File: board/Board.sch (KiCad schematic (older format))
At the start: 62 parts, among them J1 CONN_02X10, J10 CONN_01X03, J11 CONN_01X03, J12 CONN_01X02, J15 GS3, J16 GS3, J17 GS3, J18 GS2, J19 CONN_01X01, J2 CONN_01X03, J3 CONN_01X03, J4 CONN_01X03, J5 CONN_01X03, J6 CONN_01X03, J7 CONN_01X03, J8 CONN_01X03, J9 CONN_01X03, SW1 SW_Push, U1 STM32F410RBTx, U2 LF33ABDT-TR, U3 ICM-20689, U4 SN74LVC1G04, U5 MS5637, U6 MAG3110, Y1 25 MHz

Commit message: decouple cap
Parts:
- added C3: 100nF, Capacitors_SMD:C_0805_HandSoldering, symbol C
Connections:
- net GND: now also C3.2
- net VCC: now also C3.1

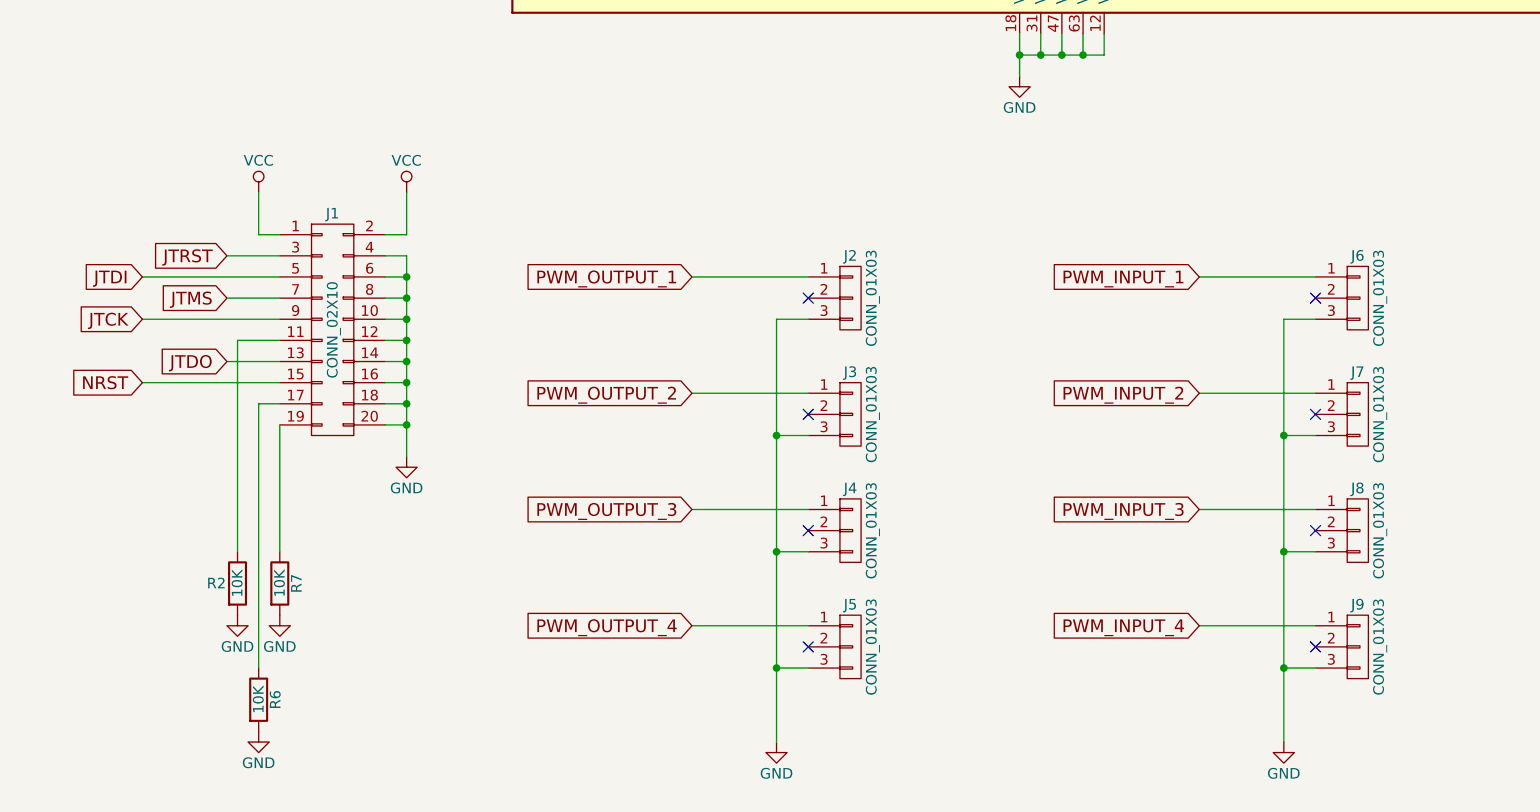
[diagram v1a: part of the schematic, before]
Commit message: smaller JTAG pin
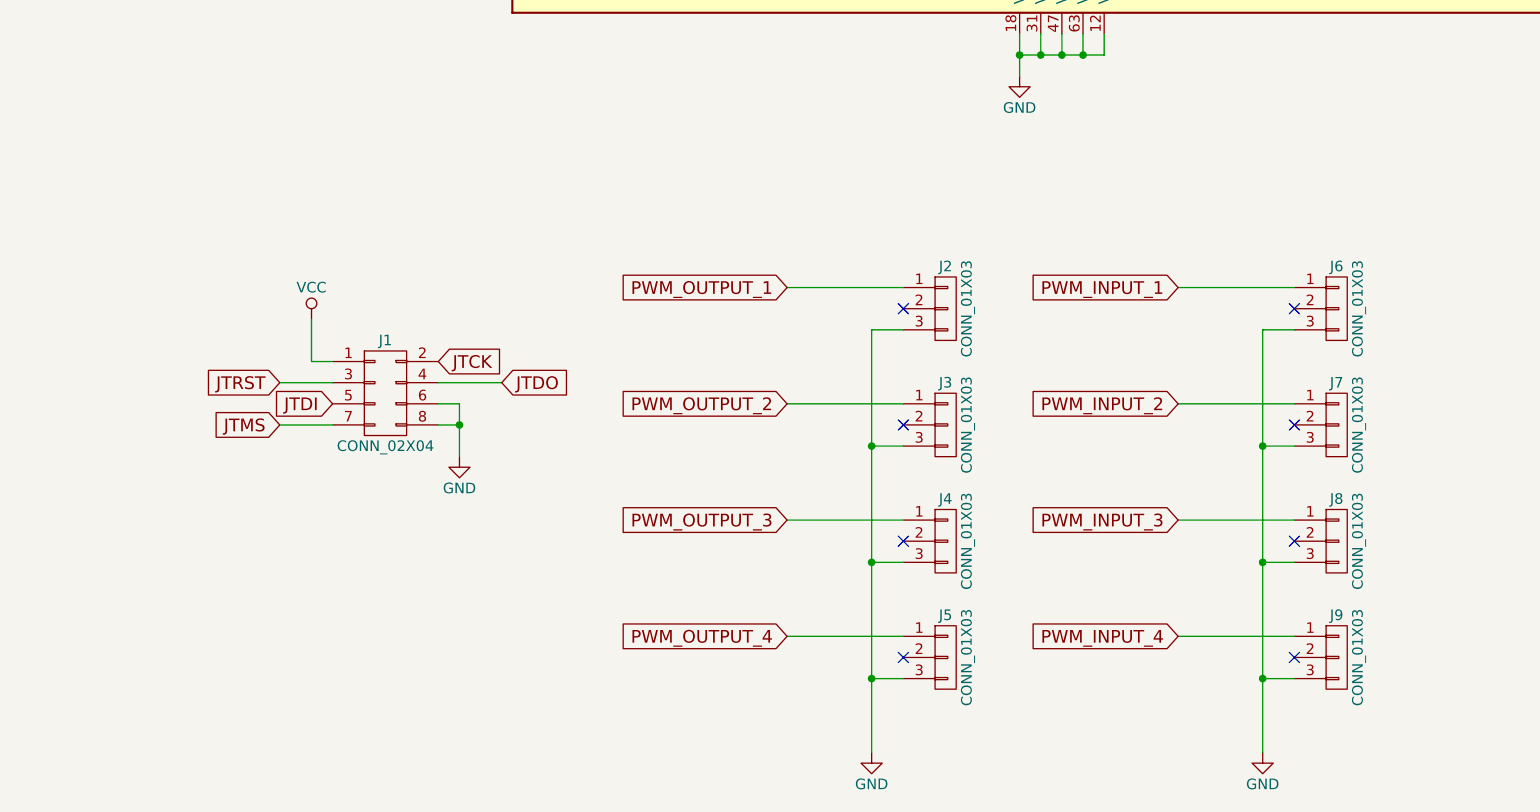
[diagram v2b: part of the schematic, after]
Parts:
- removed J1: CONN_02X10, Connect:IDC_Header_Straight_20pins, symbol CONN_02X10
- removed R2, R6, R7: 10K, Resistors_SMD:R_0805_HandSoldering, symbol R
- added J1: CONN_02X04, Pin_Headers:Pin_Header_Straight_2x04_Pitch2.54mm, symbol CONN_02X04
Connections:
- net GND: now also J1.6 (P6), J1.8 (P8)
- net JTCK: now also J1.2 (P2)
- net JTDI: now also J1.5 (P5)
- net JTDO: now also J1.4 (P4)
- net JTMS: now also J1.7 (P7)
- net JTRST: now also J1.3 (P3)
- net VCC: now also J1.1 (P1)
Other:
- moved on the sheet: J2, J3, J4, J5, J6, J7, J8, J9

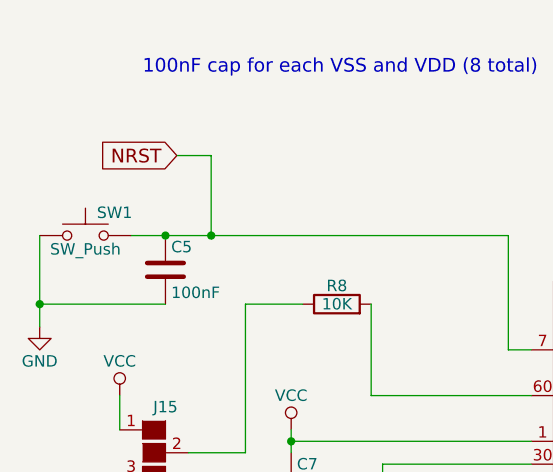
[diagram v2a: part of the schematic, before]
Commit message: removed NRST global labl
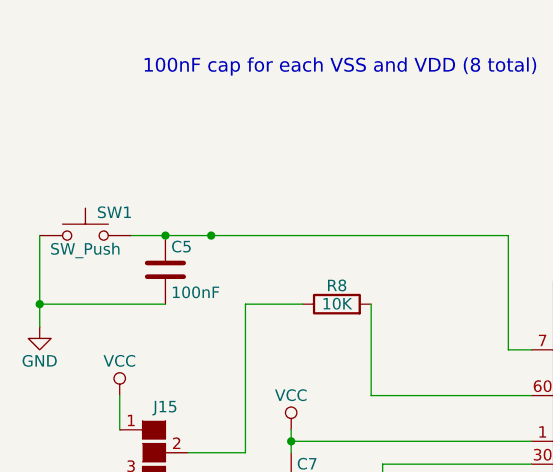
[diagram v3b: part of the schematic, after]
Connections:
- net NRST: no longer names the net of C5.1, SW1.2, U1.7 (NRST)

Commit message: new pcb
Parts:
- renumbered C16 to C10, C17 to C11, C18 to C12, C19 to C13, C3 to C14, C4 to C15, C20 to C16, C6 to C17, C21 to C18, C13 to C19, C22 to C20, C14 to C21, C23 to C22, C15 to C23, C5 to C3, C7 to C4, C9 to C5, C8 to C6, C10 to C7, C11 to C8, C12 to C9, J15 to J1, J9 to J10, J10 to J11, J17 to J12, J16 to J13, J12 to J14, J11 to J15, J18 to J16, J19 to J17, J1 to J2, J2 to J3, J3 to J4, J4 to J5, J5 to J6, J6 to J7, J7 to J8, J8 to J9, R3 to R2, R8 to R3, R9 to R4, R10 to R5, R11 to R6, R12 to R7, R4 to R8, R5 to R9, U4 to U2, U2 to U3, U3 to U4, U6 to U5, U5 to U6

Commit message: assigned the new footprint
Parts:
- U1: footprint Housings_QFP:LQFP-64_10x10mm_Pitch0.5mm -> Local_prints:LQFP-64_10x10mm_Pitch0.5mm_handsoldering

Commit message: organized the board a bit
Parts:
- added R10, R11: 10K, Resistors_SMD:R_0805_HandSoldering, symbol R
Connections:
- net VCC: now also R10.1, R11.1
- net I2C2_SCL: now reaches U1.29 (FMPI2C1_SCL/I2C2_SCL/I2S1_MCK/I2S2_CK/SPI2_SCK/PB10)
- net I2C2_SCL: now also U5.7 (SCL), U6.3 (SCL), R11.2
- net I2C2_SDA: now reaches U1.54 (ADC1_EXTI11/I2C2_SDA/I2S_CKIN/SYS_TRACED3/TIM5_CH4/PB11)
- net I2C2_SDA: now also U5.6 (SDA), U6.2 (SDA), R10.2
- net I2C_SCL renamed I2C1_SCL
- net I2C1_SCL: no longer U5.7 (SCL), U6.3 (SCL)
- net I2C_SDA renamed I2C1_SDA
- net I2C1_SDA: no longer U5.6 (SDA), U6.2 (SDA)
- no-connect marks 30 -> 28
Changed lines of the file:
@@
 $EndComp
 Text GLabel 8600 4550 2    60   Input ~ 0
-I2C_SDA
-Text GLabel 9050 4450 2    60   Input ~ 0
-I2C_SCL
+I2C1_SDA
+Text GLabel 9100 4450 2    60   Input ~ 0
+I2C1_SCL
 Text GLabel 8600 4350 2    60   Input ~ 0
 UART_RX
-Text GLabel 9050 4250 2    60   Input ~ 0
+Text GLabel 9100 4250 2    60   Input ~ 0
 UART_TX
 $Comp
@@
 $EndComp
 Text GLabel 9000 6850 0    60   Input ~ 0
-I2C_SDA
+I2C1_SDA
 Text GLabel 8500 6750 0    60   Input ~ 0
-I2C_SCL
+I2C1_SCL
 $Comp
 L GND #PWR027
@@
 	1    0    0    -1
 $EndComp
-NoConn ~ 8200 4650
 NoConn ~ 8200 3750
 NoConn ~ 8200 3650
@@
 NoConn ~ 2800 4950
 NoConn ~ 8200 3150
-NoConn ~ 8200 4750
 NoConn ~ 8200 4150
 Text GLabel 12950 4850 0    60   Input ~ 0
-I2C_SCL
+I2C2_SCL
 Text GLabel 13400 4750 0    60   Input ~ 0
-I2C_SDA
+I2C2_SDA
 $Comp
 L VCC #PWR037
@@
 MAG_INT
 Text GLabel 12850 6200 0    60   Input ~ 0
-I2C_SDA
+I2C2_SDA
 Text GLabel 12400 6100 0    60   Input ~ 0
-I2C_SCL
+I2C2_SCL
 $Comp
 L C C15
@@
 Wire Wire Line
 	14100 2650 15250 2650
-Connection ~ 1400 1450
 Wire Wire Line
 	1300 3850 2050 3850
@@
 	8200 4550 8600 4550
 Wire Wire Line
-	9050 4450 8200 4450
+	8200 4450 9100 4450
 Wire Wire Line
 	8200 4350 8600 4350
 Wire Wire Line
-	9050 4250 8200 4250
+	8200 4250 9100 4250
 Wire Wire Line
 	8500 6750 9250 6750
@@
 	2550 7400 2650 7400
 Connection ~ 2650 7400
+Text GLabel 10800 4750 2    60   Input ~ 0
+I2C2_SDA
+Wire Wire Line
+	8200 4650 11350 4650
+Text GLabel 11350 4650 2    60   Input ~ 0
+I2C2_SCL
+Wire Wire Line
+	8200 4750 10800 4750
+$Comp
+L R R11
+U 1 1 58FA170E
+P 10650 4300
+F 0 "R11" V 10730 4300 50  0000 C CNN
+F 1 "10K" V 10650 4300 50  0000 C CNN
+F 2 "Resistors_SMD:R_0805_HandSoldering" V 10580 4300 50  0001 C CNN
+F 3 "" H 10650 4300 50  0001 C CNN
+	1    10650 4300
+	1    0    0    -1
+$EndComp
+$Comp
+L R R10
+U 1 1 58FA180F
+P 10450 4300
+F 0 "R10" V 10530 4300 50  0000 C CNN
+F 1 "10K" V 10450 4300 50  0000 C CNN
+F 2 "Resistors_SMD:R_0805_HandSoldering" V 10380 4300 50  0001 C CNN
+F 3 "" H 10450 4300 50  0001 C CNN
+	1    10450 4300
+	1    0    0    -1
+$EndComp
+Wire Wire Line
+	10450 4450 10450 4750
+Connection ~ 10450 4750
+Wire Wire Line
+	10650 4450 10650 4650
+Connection ~ 10650 4650
+$Comp
+L VCC #PWR044
+U 1 1 58FA1F57
+P 10550 4000
+F 0 "#PWR044" H 10550 3850 50  0001 C CNN
+F 1 "VCC" H 10550 4150 50  0000 C CNN
+F 2 "" H 10550 4000 50  0001 C CNN
+F 3 "" H 10550 4000 50  0001 C CNN
+	1    10550 4000
+	1    0    0    -1
+$EndComp
+Wire Wire Line
+	10450 4150 10650 4150
+Wire Wire Line
+	10550 4150 10550 4000
+Connection ~ 10550 4150
 $EndSCHEMATC

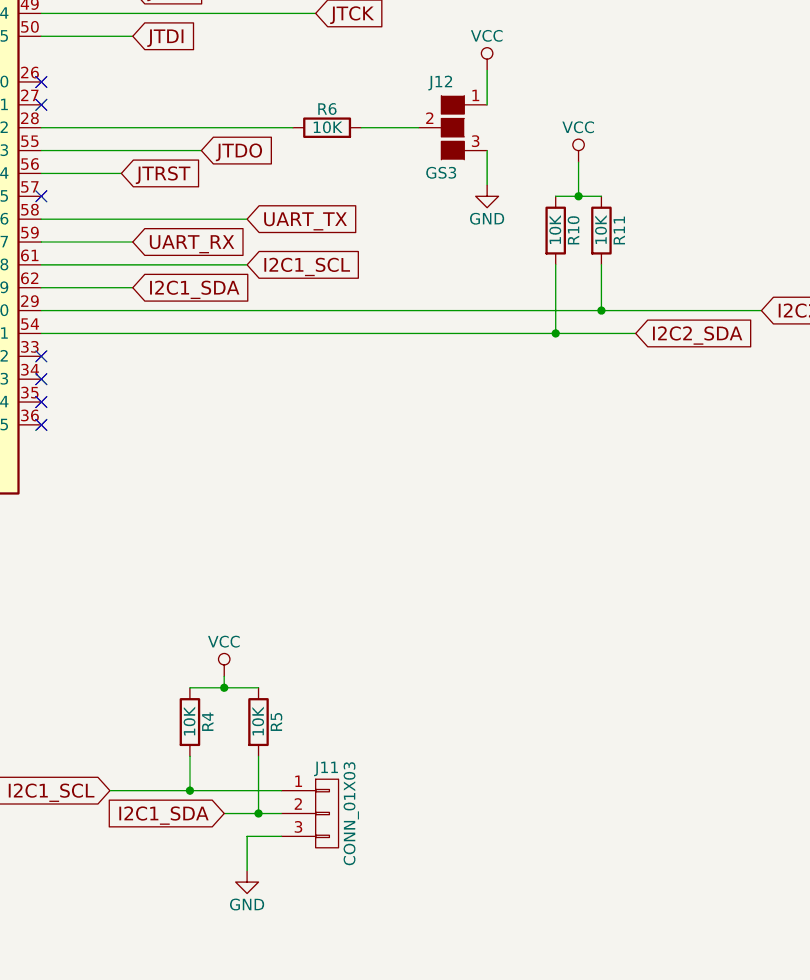
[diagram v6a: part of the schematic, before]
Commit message: using resistor array for I2C pullups
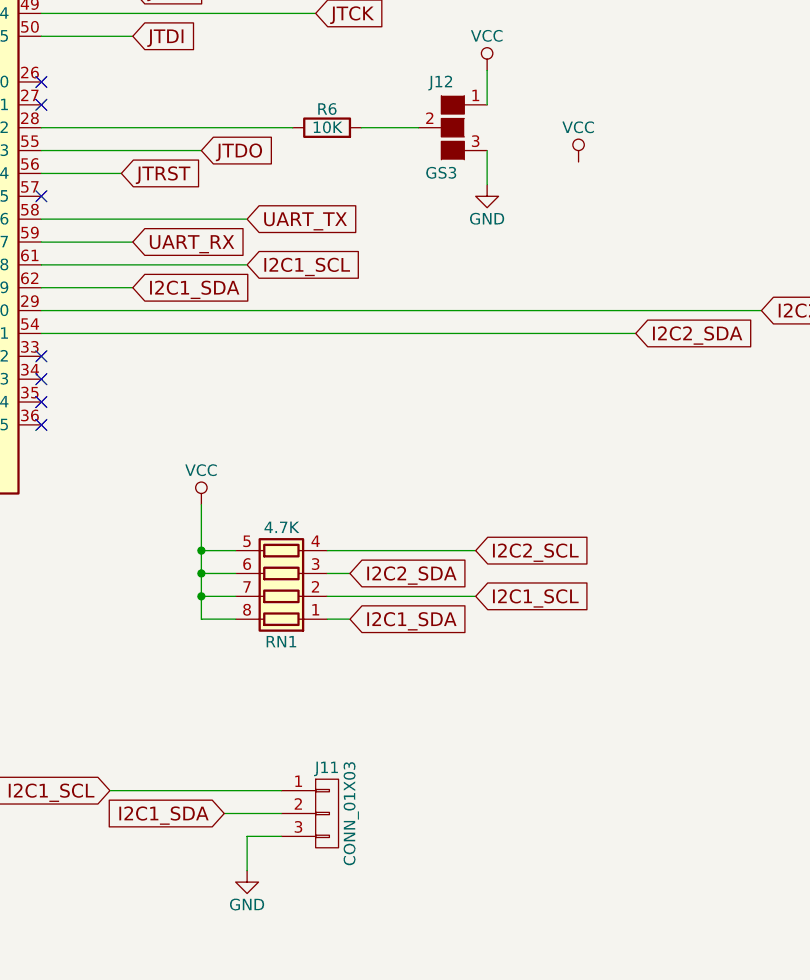
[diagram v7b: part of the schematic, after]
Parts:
- removed R10, R11, R4, R5: 10K, Resistors_SMD:R_0805_HandSoldering, symbol R
- added RN1: 4.7K, Resistors_SMD:R_Array_Convex_4x1206, symbol R_Pack04
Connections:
- net I2C1_SCL: now also RN1.2 (R2.1)
- net I2C1_SDA: now also RN1.1 (R1.1)
- net I2C2_SCL: now also RN1.4 (R4.1)
- net I2C2_SDA: now also RN1.3 (R3.1)
- net VCC: now also RN1.5 (R4.2), RN1.6 (R3.2), RN1.7 (R2.2), RN1.8 (R1.2)
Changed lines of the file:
@@
 UART_RX
 $Comp
-L R R4
-U 1 1 58D9A242
-P 8850 6450
-F 0 "R4" V 8930 6450 50  0000 C CNN
-F 1 "10K" V 8850 6450 50  0000 C CNN
-F 2 "Resistors_SMD:R_0805_HandSoldering" V 8780 6450 50  0001 C CNN
-F 3 "" H 8850 6450 50  0001 C CNN
-	1    8850 6450
-	1    0    0    -1
-$EndComp
-$Comp
-L R R5
-U 1 1 58D9A495
-P 9150 6450
-F 0 "R5" V 9230 6450 50  0000 C CNN
-F 1 "10K" V 9150 6450 50  0000 C CNN
-F 2 "Resistors_SMD:R_0805_HandSoldering" V 9080 6450 50  0001 C CNN
-F 3 "" H 9150 6450 50  0001 C CNN
-	1    9150 6450
-	1    0    0    -1
-$EndComp
-$Comp
-L VCC #PWR028
-U 1 1 58D9B26E
-P 9000 6250
-F 0 "#PWR028" H 9000 6100 50  0001 C CNN
-F 1 "VCC" H 9000 6400 50  0000 C CNN
-F 2 "" H 9000 6250 50  0001 C CNN
-F 3 "" H 9000 6250 50  0001 C CNN
-	1    9000 6250
-	1    0    0    -1
-$EndComp
-$Comp
-L PWR_FLAG #FLG029
+L PWR_FLAG #FLG028
 U 1 1 58DB2A85
 P 11150 1500
-F 0 "#FLG029" H 11150 1575 50  0001 C CNN
+F 0 "#FLG028" H 11150 1575 50  0001 C CNN
 F 1 "PWR_FLAG" H 10950 1650 50  0000 C CNN
 F 2 "" H 11150 1500 50  0001 C CNN
@@
 $EndComp
 $Comp
-L PWR_FLAG #FLG030
+L PWR_FLAG #FLG029
 U 1 1 58DB1674
 P 11250 1000
-F 0 "#FLG030" H 11250 1075 50  0001 C CNN
+F 0 "#FLG029" H 11250 1075 50  0001 C CNN
 F 1 "PWR_FLAG" H 11250 1150 50  0000 C CNN
 F 2 "" H 11250 1000 50  0001 C CNN
@@
 $EndComp
 $Comp
-L GND #PWR031
+L GND #PWR030
 U 1 1 58DB0976
 P 6450 8950
-F 0 "#PWR031" H 6450 8700 50  0001 C CNN
+F 0 "#PWR030" H 6450 8700 50  0001 C CNN
 F 1 "GND" H 6450 8800 50  0000 C CNN
 F 2 "" H 6450 8950 50  0001 C CNN
@@
 $EndComp
 $Comp
-L VCC #PWR032
+L VCC #PWR031
 U 1 1 58F60FBC
 P 8900 8050
-F 0 "#PWR032" H 8900 7900 50  0001 C CNN
+F 0 "#PWR031" H 8900 7900 50  0001 C CNN
 F 1 "VCC" H 8900 8200 50  0000 C CNN
 F 2 "" H 8900 8050 50  0001 C CNN
@@
 $EndComp
 $Comp
-L GND #PWR033
+L GND #PWR032
 U 1 1 58F61042
 P 8900 8650
-F 0 "#PWR033" H 8900 8400 50  0001 C CNN
+F 0 "#PWR032" H 8900 8400 50  0001 C CNN
 F 1 "GND" H 8900 8500 50  0000 C CNN
 F 2 "" H 8900 8650 50  0001 C CNN
@@
 $EndComp
 $Comp
-L GND #PWR034
+L GND #PWR033
 U 1 1 58F6AF97
 P 15000 1900
-F 0 "#PWR034" H 15000 1650 50  0001 C CNN
+F 0 "#PWR033" H 15000 1650 50  0001 C CNN
 F 1 "GND" H 15000 1750 50  0000 C CNN
 F 2 "" H 15000 1900 50  0001 C CNN
@@
 $EndComp
 $Comp
-L +BATT #PWR035
+L +BATT #PWR034
 U 1 1 58F72A6D
 P 11550 1000
-F 0 "#PWR035" H 11550 850 50  0001 C CNN
+F 0 "#PWR034" H 11550 850 50  0001 C CNN
 F 1 "+BATT" H 11550 1140 50  0000 C CNN
 F 2 "" H 11550 1000 50  0001 C CNN
@@
 $EndComp
 $Comp
-L +BATT #PWR036
+L +BATT #PWR035
 U 1 1 58F73262
 P 14400 800
-F 0 "#PWR036" H 14400 650 50  0001 C CNN
+F 0 "#PWR035" H 14400 650 50  0001 C CNN
 F 1 "+BATT" H 14400 940 50  0000 C CNN
 F 2 "" H 14400 800 50  0001 C CNN
@@
 I2C2_SDA
 $Comp
-L VCC #PWR037
+L VCC #PWR036
 U 1 1 58F863D2
 P 12150 4500
-F 0 "#PWR037" H 12150 4350 50  0001 C CNN
+F 0 "#PWR036" H 12150 4350 50  0001 C CNN
 F 1 "VCC" H 12150 4650 50  0000 C CNN
 F 2 "" H 12150 4500 50  0001 C CNN
@@
 $EndComp
 $Comp
-L GND #PWR038
+L GND #PWR037
 U 1 1 58F86E8C
 P 12150 5100
-F 0 "#PWR038" H 12150 4850 50  0001 C CNN
+F 0 "#PWR037" H 12150 4850 50  0001 C CNN
 F 1 "GND" H 12150 4950 50  0000 C CNN
 F 2 "" H 12150 5100 50  0001 C CNN
@@
 $EndComp
 $Comp
-L GND #PWR039
+L GND #PWR038
 U 1 1 58F9DAF3
 P 12400 7000
-F 0 "#PWR039" H 12400 6750 50  0001 C CNN
+F 0 "#PWR038" H 12400 6750 50  0001 C CNN
 F 1 "GND" H 12400 6850 50  0000 C CNN
 F 2 "" H 12400 7000 50  0001 C CNN
@@
 $EndComp
 $Comp
-L VCC #PWR040
+L VCC #PWR039
 U 1 1 58FA1A71
 P 14100 5800
-F 0 "#PWR040" H 14100 5650 50  0001 C CNN
+F 0 "#PWR039" H 14100 5650 50  0001 C CNN
 F 1 "VCC" H 14100 5950 50  0000 C CNN
 F 2 "" H 14100 5800 50  0001 C CNN
@@
 $EndComp
 $Comp
-L GND #PWR041
+L GND #PWR040
 U 1 1 58FA2856
 P 15050 6450
-F 0 "#PWR041" H 15050 6200 50  0001 C CNN
+F 0 "#PWR040" H 15050 6200 50  0001 C CNN
 F 1 "GND" H 15050 6300 50  0000 C CNN
 F 2 "" H 15050 6450 50  0001 C CNN
@@
 $EndComp
 $Comp
-L VCC #PWR042
+L VCC #PWR041
 U 1 1 58F99C24
 P 1950 6900
-F 0 "#PWR042" H 1950 6750 50  0001 C CNN
+F 0 "#PWR041" H 1950 6750 50  0001 C CNN
 F 1 "VCC" H 1950 7050 50  0000 C CNN
 F 2 "" H 1950 6900 50  0001 C CNN
@@
 	1    0    0    -1
 $EndComp
+$Comp
+L GND #PWR042
+U 1 1 58F9E5CF
+P 2650 7550
+F 0 "#PWR042" H 2650 7300 50  0001 C CNN
+F 1 "GND" H 2650 7400 50  0000 C CNN
+F 2 "" H 2650 7550 50  0001 C CNN
+F 3 "" H 2650 7550 50  0001 C CNN
+	1    2650 7550
+	1    0    0    -1
+$EndComp
+Text GLabel 10800 4750 2    60   Input ~ 0
+I2C2_SDA
+Text GLabel 11350 4650 2    60   Input ~ 0
+I2C2_SCL
+$Comp
+L VCC #PWR043
+U 1 1 58FA1F57
+P 10550 4000
+F 0 "#PWR043" H 10550 3850 50  0001 C CNN
+F 1 "VCC" H 10550 4150 50  0000 C CNN
+F 2 "" H 10550 4000 50  0001 C CNN
+F 3 "" H 10550 4000 50  0001 C CNN
+	1    10550 4000
+	1    0    0    -1
+$EndComp
+$Comp
+L R_Pack04 RN1
+U 1 1 58FD5E70
+P 9250 5800
+F 0 "RN1" V 8950 5800 50  0000 C CNN
+F 1 "4.7K" V 9450 5800 50  0000 C CNN
+F 2 "Resistors_SMD:R_Array_Convex_4x1206" V 9525 5800 50  0001 C CNN
+F 3 "" H 9250 5800 50  0001 C CNN
+	1    9250 5800
+	0    -1   -1   0
+$EndComp
+Text GLabel 9550 5800 2    60   Input ~ 0
+I2C2_SDA
+Text GLabel 10100 5700 2    60   Input ~ 0
+I2C2_SCL
+Text GLabel 10100 5900 2    60   Input ~ 0
+I2C1_SCL
+Text GLabel 9550 6000 2    60   Input ~ 0
+I2C1_SDA
+$Comp
+L VCC #PWR044
+U 1 1 58FDBFEC
+P 8900 5500
+F 0 "#PWR044" H 8900 5350 50  0001 C CNN
+F 1 "VCC" H 8900 5650 50  0000 C CNN
+F 2 "" H 8900 5500 50  0001 C CNN
+F 3 "" H 8900 5500 50  0001 C CNN
+	1    8900 5500
+	1    0    0    -1
+$EndComp
 Wire Wire Line
 	8600 3050 8200 3050
@@
 Wire Wire Line
 	10800 8050 10800 8200
-Wire Wire Line
-	9150 6600 9150 6850
-Connection ~ 9150 6850
-Wire Wire Line
-	8850 6600 8850 6750
-Connection ~ 8850 6750
-Wire Wire Line
-	8850 6300 9150 6300
-Wire Wire Line
-	9000 6300 9000 6250
-Connection ~ 9000 6300
 Connection ~ 11250 1200
 Wire Wire Line
@@
 Wire Wire Line
 	2550 7200 2850 7200
-$Comp
-L GND #PWR043
-U 1 1 58F9E5CF
-P 2650 7550
-F 0 "#PWR043" H 2650 7300 50  0001 C CNN
-F 1 "GND" H 2650 7400 50  0000 C CNN
-F 2 "" H 2650 7550 50  0001 C CNN
-F 3 "" H 2650 7550 50  0001 C CNN
-	1    2650 7550
-	1    0    0    -1
-$EndComp
 Wire Wire Line
 	2550 7300 2650 7300
@@
 	2550 7400 2650 7400
 Connection ~ 2650 7400
-Text GLabel 10800 4750 2    60   Input ~ 0
-I2C2_SDA
 Wire Wire Line
 	8200 4650 11350 4650
-Text GLabel 11350 4650 2    60   Input ~ 0
-I2C2_SCL
 Wire Wire Line
 	8200 4750 10800 4750
-$Comp
-L R R11
-U 1 1 58FA170E
-P 10650 4300
-F 0 "R11" V 10730 4300 50  0000 C CNN
-F 1 "10K" V 10650 4300 50  0000 C CNN
-F 2 "Resistors_SMD:R_0805_HandSoldering" V 10580 4300 50  0001 C CNN
-F 3 "" H 10650 4300 50  0001 C CNN
-	1    10650 4300
-	1    0    0    -1
-$EndComp
-$Comp
-L R R10
-U 1 1 58FA180F
-P 10450 4300
-F 0 "R10" V 10530 4300 50  0000 C CNN
-F 1 "10K" V 10450 4300 50  0000 C CNN
-F 2 "Resistors_SMD:R_0805_HandSoldering" V 10380 4300 50  0001 C CNN
-F 3 "" H 10450 4300 50  0001 C CNN
-	1    10450 4300
-	1    0    0    -1
-$EndComp
-Wire Wire Line
-	10450 4450 10450 4750
-Connection ~ 10450 4750
-Wire Wire Line
-	10650 4450 10650 4650
-Connection ~ 10650 4650
-$Comp
-L VCC #PWR044
-U 1 1 58FA1F57
-P 10550 4000
-F 0 "#PWR044" H 10550 3850 50  0001 C CNN
-F 1 "VCC" H 10550 4150 50  0000 C CNN
-F 2 "" H 10550 4000 50  0001 C CNN
-F 3 "" H 10550 4000 50  0001 C CNN
-	1    10550 4000
-	1    0    0    -1
-$EndComp
-Wire Wire Line
-	10450 4150 10650 4150
-Wire Wire Line
-	10550 4150 10550 4000
-Connection ~ 10550 4150
+Wire Wire Line
+	10100 5900 9450 5900
+Wire Wire Line
+	9450 6000 9550 6000
+Wire Wire Line
+	10100 5700 9450 5700
+Wire Wire Line
+	9450 5800 9550 5800
+Wire Wire Line
+	8900 5500 8900 6000
+Wire Wire Line
+	8900 6000 9050 6000
+Wire Wire Line
+	9050 5900 8900 5900
+Connection ~ 8900 5900
+Wire Wire Line
+	9050 5800 8900 5800
+Connection ~ 8900 5800
+Wire Wire Line
+	9050 5700 8900 5700
+Connection ~ 8900 5700
 $EndSCHEMATC
